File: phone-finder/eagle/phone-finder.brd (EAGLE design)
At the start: 50 x 50 mm, 46 parts, among them J1 MICRO USB, J2 PHONE-JACK, K1 RELAY, Q1 12Mhz, Q2 2N2222, Q3 2N2222, T1 DTA114EET1G (2x10K), U1 AP2114H-3.3TRG1, U2 NUF2042XV6T1G, U3 LPC11U35FHI33/501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

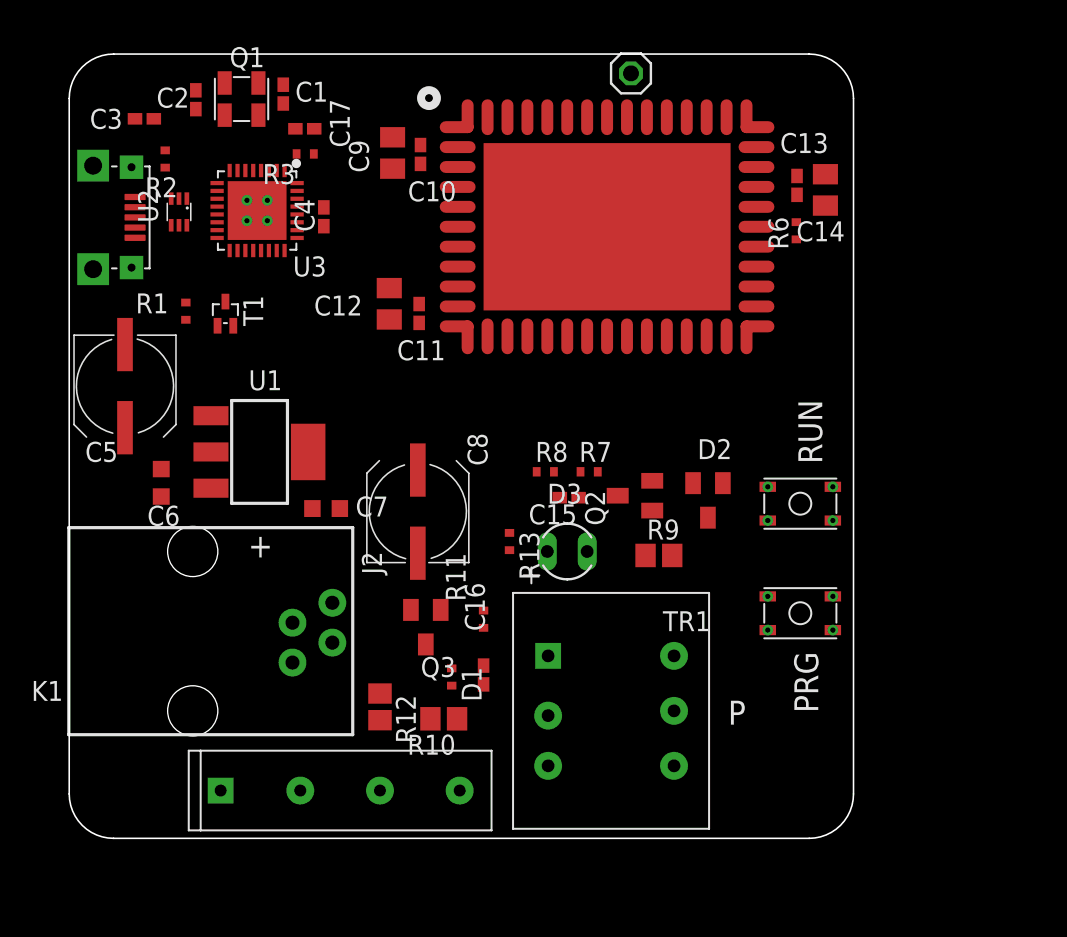
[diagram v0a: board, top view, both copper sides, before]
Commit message: Updated BOM (still needs Mouser part numbers and part references).
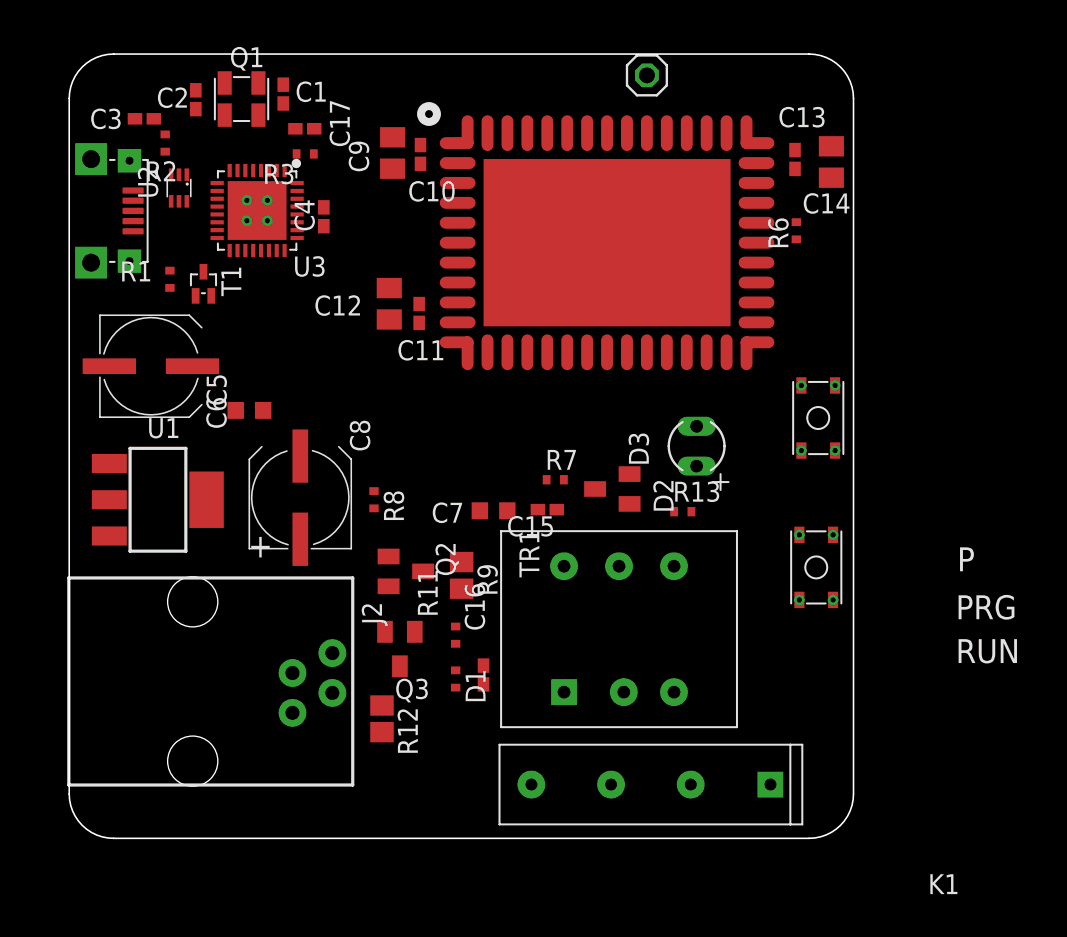
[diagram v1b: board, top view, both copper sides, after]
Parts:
- removed R10: 100, phone-finder:R0805
- moved K1 19.8 mm to (37.1, 3.43), turned to 180 degrees
- moved Q2 15.4 mm to (21.5, 17.0), turned to 270 degrees
- moved R9 12.6 mm to (25.0, 16.8), turned to 270 degrees
- moved R13 11.2 mm to (39.1, 20.8), turned to 0 degrees
- moved R8 11.1 mm to (19.4, 21.6), turned to 270 degrees
- moved C7 10.7 mm to (27.1, 20.9), turned to 0 degrees
- moved D3 10.6 mm to (40.0, 25.0), turned to 90 degrees
- moved C8 7.55 mm to (14.7, 21.7)
- moved C6 7.28 mm to (11.5, 27.3), turned to 0 degrees
- moved U1 7.16 mm to (5.66, 21.6)
- moved D2 6.14 mm to (34.6, 22.3), turned to 90 degrees
- moved S2 5.58 mm to (47.8, 26.8), turned to 90 degrees
- moved TR1 5.23 mm to (35.1, 13.3), turned to 270 degrees
- moved J2 3.21 mm to (7.87, 10.0)
- moved S1 3.09 mm to (47.6, 17.3), turned to 270 degrees
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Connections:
- removed net N$15: D1.2, R10.2, R12.1
- net N$9: now also D1.2, R12.1; no longer R10.1
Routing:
- net GND: track 0.00 -> 33.5 mm

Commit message: PCB layout in progress.
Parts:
- moved C7 18.2 mm to (9.65, 26.2), turned to 180 degrees
- moved C6 6.17 mm to (5.40, 26.3), turned to 180 degrees
- moved C3 4.89 mm to (9.62, 45.1)
- moved S2 4.83 mm to (47.8, 22.0)
- moved K1 4.06 mm to (33.0, 3.43)
- moved S1 3.94 mm to (47.6, 13.3)
- moved C2 2.71 mm to (10.7, 47.6)
- moved R1 2.37 mm to (7.41, 37.8), turned to 0 degrees
- moved R2 2.25 mm to (7.62, 42.6), turned to 0 degrees
- moved Q1 2.19 mm to (13.1, 47.5)
- moved C1 2.04 mm to (15.7, 47.6)
- moved C11 1.21 mm to (22.4, 32.3)
- moved U2 1.17 mm to (7.25, 40.3)
- moved R6 1.14 mm to (46.4, 39.9)
- moved R3 0.92 mm to (15.9, 43.9)
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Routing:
- net GND: track 33.5 -> 358.0 mm, vias 0 -> 18
- net +3V3: track 0.00 -> 43.0 mm, vias 0 -> 6
- net +5V: track 0.00 -> 34.0 mm, vias 0 -> 4
- net N$1: track 0.00 -> 8.47 mm
- net N$6: track 0.00 -> 6.94 mm
- net N$3: track 0.00 -> 6.16 mm
- net USB_DM: track 0.00 -> 5.23 mm
- net N$12: track 0.00 -> 3.87 mm
- net N$2: track 0.00 -> 3.43 mm
- net USB_DP: track 0.00 -> 3.13 mm
- net WIFI_IRQ: track 0.00 -> 1.28 mm, vias 0 -> 1
- net LED: track 0.00 -> 1.20 mm, vias 0 -> 1
- added copper zone on layer 16, net GND

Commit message: Layout work in progress.
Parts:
- moved R12 23.9 mm to (43.4, 3.17), turned to 180 degrees
- moved D1 18.6 mm to (42.8, 6.35)
- moved C16 18.5 mm to (44.5, 6.22)
- moved R7 8.91 mm to (22.1, 21.7), turned to 180 degrees
- moved C15 8.58 mm to (22.1, 18.9), turned to 0 degrees
- moved R9 5.10 mm to (27.3, 21.3), turned to 180 degrees
- moved R11 3.87 mm to (21.0, 11.8), turned to 180 degrees
- moved R13 3.76 mm to (36.0, 23.0)
- moved K1 3.43 mm to (29.6, 3.43)
- moved D2 3.20 mm to (31.9, 23.9)
- moved Q3 3.18 mm to (21.8, 8.97), turned to 90 degrees
- moved R8 3.00 mm to (22.1, 20.3), turned to 180 degrees
- moved R3 2.13 mm to (18.0, 44.5)
- moved R6 1.94 mm to (48.3, 39.5), turned to 270 degrees
- moved C17 1.85 mm to (17.7, 45.7)
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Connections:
- removed net N$20: K1.4, R12.2
- new net N$15: K1.1, R12.2
- net +3V3: no longer U1.2
- net N$11: now also K1.4; no longer K1.1
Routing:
- net +3V3: track 43.0 -> 95.5 mm, vias 6 -> 8
- net GND: track 358.0 -> 385.3 mm, vias 18 -> 22
- net +5V: track 34.0 -> 32.9 mm
- net N$6: track 6.94 -> 6.24 mm
- net N$12: track 3.87 -> 3.35 mm

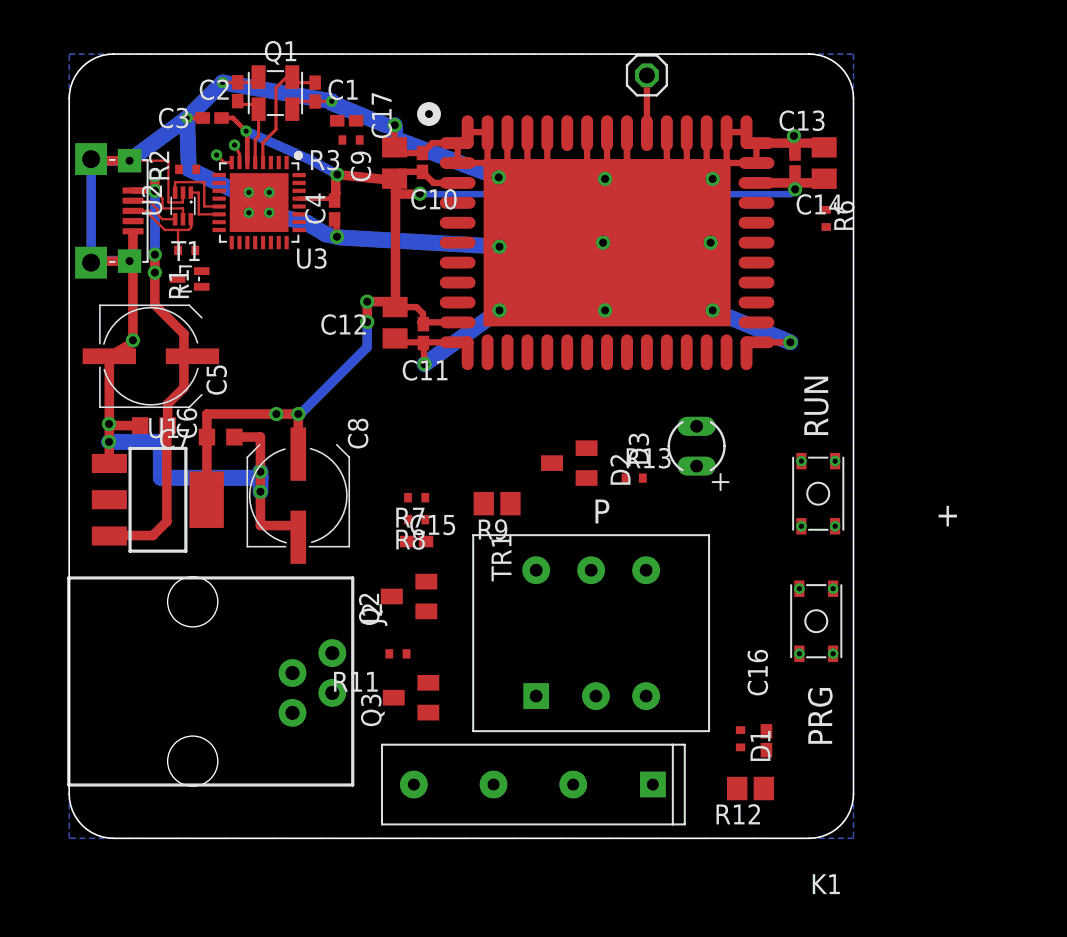
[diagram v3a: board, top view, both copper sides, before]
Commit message: Critical net routing done.
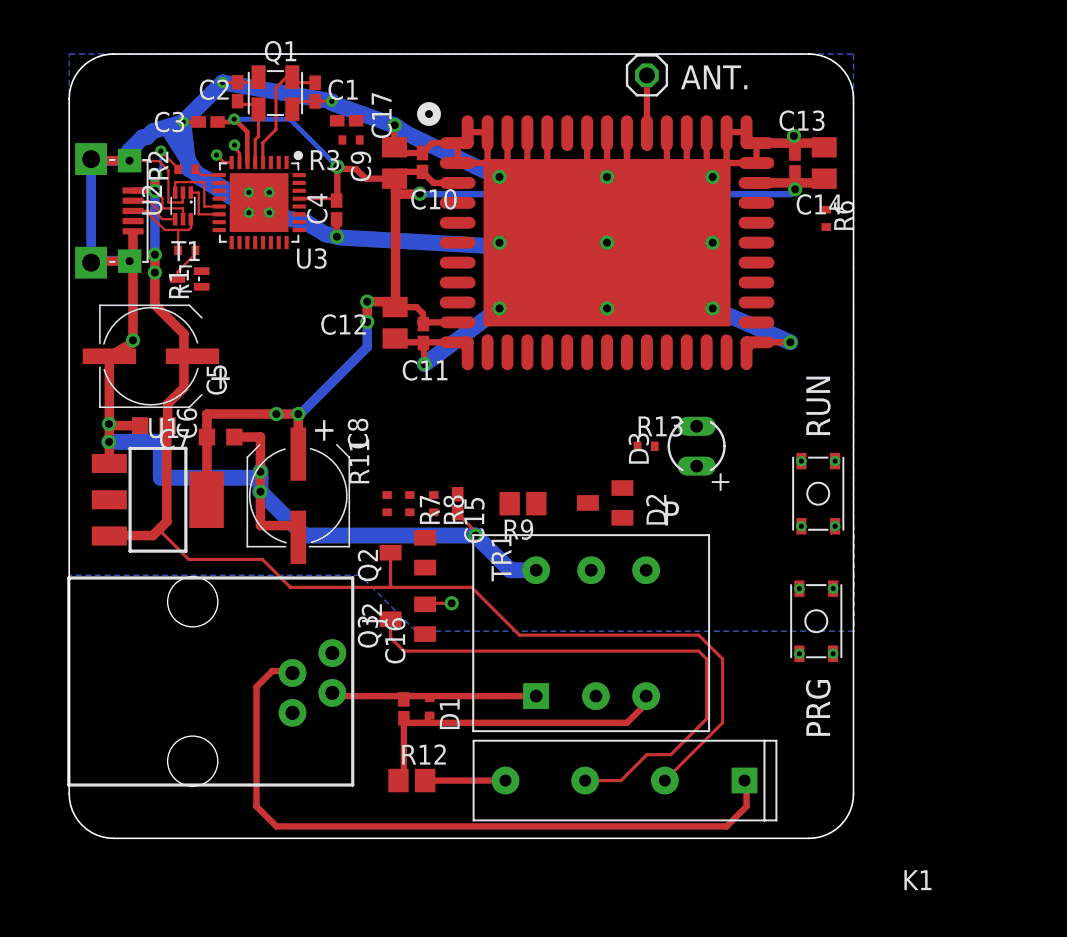
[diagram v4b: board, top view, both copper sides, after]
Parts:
- moved C16 23.2 mm to (21.3, 8.26)
- moved R12 21.6 mm to (21.8, 3.68), turned to 0 degrees
- moved D1 19.9 mm to (23.0, 8.38)
- moved R11 9.60 mm to (20.3, 21.3), turned to 90 degrees
- moved K1 5.85 mm to (35.4, 3.68)
- moved Q3 5.01 mm to (21.6, 14.0)
- moved C15 3.56 mm to (24.8, 21.3), turned to 270 degrees
- moved D2 3.42 mm to (34.2, 21.4)
- moved Q2 2.80 mm to (21.6, 18.2)
- moved R13 2.17 mm to (36.8, 25.0)
- moved R9 1.65 mm to (28.9, 21.3)
- moved R8 1.49 mm to (23.2, 21.3), turned to 270 degrees
- moved R7 0.58 mm to (21.7, 21.3), turned to 270 degrees
- moved C3 0.36 mm to (8.86, 45.7)
- moved C4 0.13 mm to (17.0, 40.1)
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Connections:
- net N$11: now also K1.1; no longer K1.4
- net N$15: now also K1.4; no longer K1.1
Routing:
- net +5V: track 32.9 -> 87.2 mm, vias 4 -> 5
- net N$11: track 0.00 -> 44.2 mm
- net N$4: track 0.00 -> 35.1 mm
- net GND: track 385.3 -> 419.8 mm, vias 22 -> 24
- net N$9: track 0.00 -> 21.2 mm
- net N$10: track 0.00 -> 13.6 mm
- net N$15: track 0.00 -> 5.12 mm
- net N$5: track 0.00 -> 2.29 mm
- net +3V3: track 95.5 -> 97.5 mm
- net VBUS: track 0.00 -> 1.67 mm
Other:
- board text added: "ANT."

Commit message: Cleaned up component references.
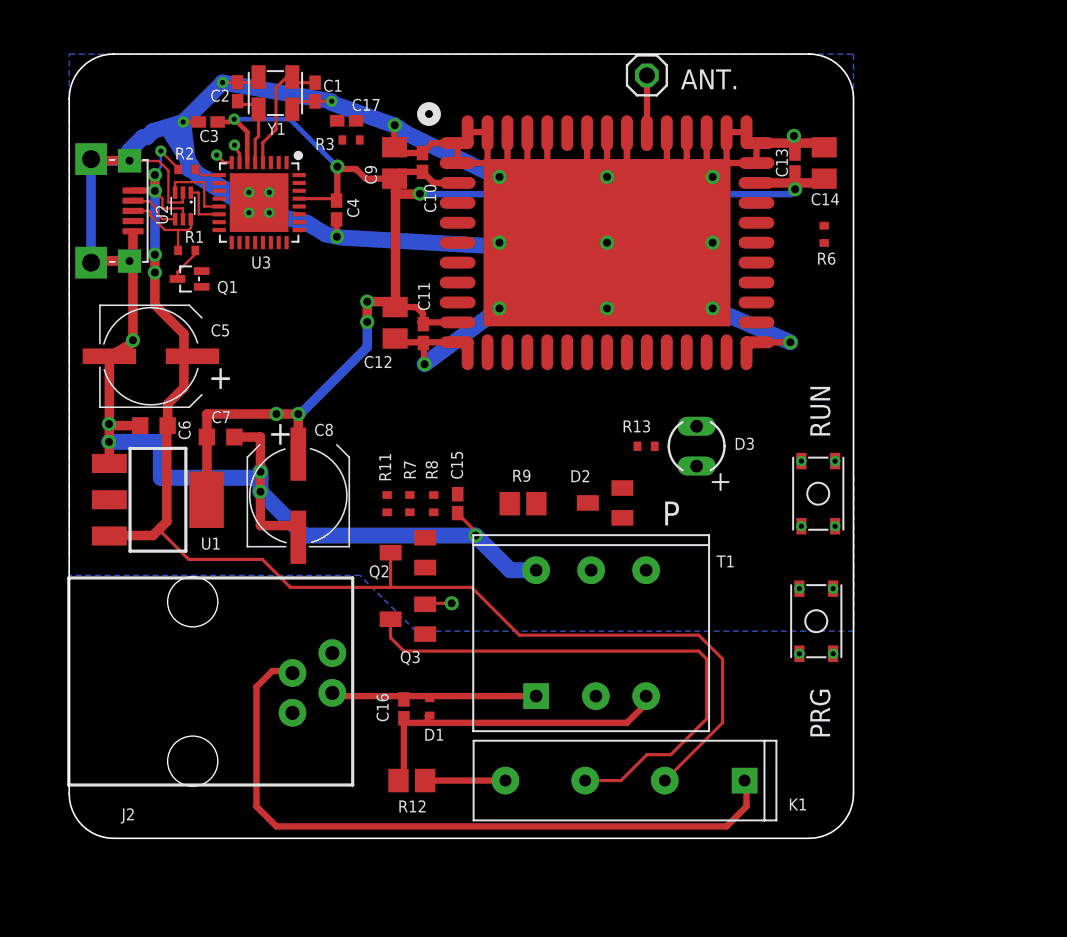
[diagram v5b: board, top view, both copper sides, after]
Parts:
- removed TR1: TRANSFORMER, phone-finder:TRANSFORMER
- added Y1: 12Mhz, phone-finder:CRYSTAL
- Q1: value 12Mhz -> DTA114EET1G (2x10K); device phone-finder:CRYSTAL -> phone-finder:SC75-BEC
- T1: value DTA114EET1G (2x10K) -> TRANSFORMER; device phone-finder:SC75-BEC -> phone-finder:TRANSFORMER
- moved T1 34.1 mm to (33.3, 13.1), turned to 270 degrees
- moved Q1 13.1 mm to (7.67, 35.7), turned to 90 degrees
- moved R6 1.02 mm to (48.1, 38.5)
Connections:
- net +3V3: now also Q1.E; no longer T1.E
- net GND: now also T1.6, Y1.2, Y1.4; no longer Q1.2, Q1.4, TR1.6
- net N$1: now also Y1.3; no longer Q1.3
- net N$10: now also T1.1; no longer TR1.1
- net N$17: now also T1.4; no longer TR1.4
- net N$3: now also Y1.1; no longer Q1.1
- net N$5: now also Q1.C; no longer T1.C
- net N$9: now also T1.3; no longer TR1.3
- net USB_CONNECT: now also Q1.B; no longer T1.B

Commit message: Added board label.
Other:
- board text added: "PHONE FINDER V1.0"
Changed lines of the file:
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@@
 <board>
 <plain>
-<text x="48.514" y="6.35" size="1.27" layer="21" font="vector" ratio="10" rot="R90">PRG</text>
-<text x="48.514" y="25.527" size="1.27" layer="21" font="vector" ratio="10" rot="R90">RUN</text>
+<text x="48.26" y="7.747" size="1.016" layer="21" font="vector" ratio="10" rot="R90">PRG</text>
+<text x="48.133" y="25.527" size="1.016" layer="21" font="vector" ratio="10" rot="R90">RUN</text>
 <text x="12.6746" y="25.0952" size="1.524" layer="21" font="vector" ratio="10">+</text>
 <wire x1="50" y1="2.828425" x2="50" y2="47.171575" width="0.1016" layer="20"/>
@@
 <wire x1="21.336" y1="10.922" x2="53.213" y2="10.922" width="0.2032" layer="42"/>
 <text x="8.8646" y="28.6512" size="1.524" layer="21" font="vector" ratio="10">+</text>
-<text x="38.989" y="47.752" size="1.27" layer="21" font="vector" ratio="10">ANT.</text>
+<text x="38.989" y="47.752" size="1.016" layer="21" font="vector" ratio="10">ANT.</text>
+<text x="3.302" y="1.143" size="1.016" layer="21" font="vector" ratio="10">PHONE FINDER V1.0</text>
 </plain>
 <attributes>
@@
 <attribute name="MF" value="" x="7.874" y="10" size="1.778" layer="27" rot="R270" display="off"/>
 <attribute name="OC_FARNELL" value="unknown" x="7.874" y="10" size="1.778" layer="27" rot="R270" display="off"/>
-<attribute name="NAME" x="3.335" y="1.143" size="0.762" layer="25" font="vector" ratio="10"/>
+<attribute name="NAME" x="18.702" y="10.668" size="0.762" layer="25" font="vector" ratio="10"/>
 </element>
 <element name="D3" library="phone-finder" package="LED" value="LED" x="40" y="25" smashed="yes" rot="R90">

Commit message: Work in progress. Minor tweaks.
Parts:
- moved R13 0.54 mm to (36.4, 25.4)
- turned D3 to 270 degrees
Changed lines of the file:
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@@
 <attribute name="NAME" x="19.615" y="41.676" size="0.762" layer="25" font="vector" ratio="10" rot="R90"/>
 </element>
-<element name="U4" library="phone-finder" package="WIFI_MODULE" value="AMW006" x="24.13" y="30.353" smashed="yes"/>
+<element name="U4" library="phone-finder" package="WIFI_MODULE" value="AMW006" x="24.13" y="30.353"/>
 <element name="C13" library="phone-finder" package="C0402K" value="0.1uF" x="46.271" y="43.053" smashed="yes" rot="R90">
 <attribute name="NAME" x="45.817" y="42.143" size="0.762" layer="25" font="vector" ratio="10" rot="R90"/>
@@
 <attribute name="NAME" x="18.702" y="10.668" size="0.762" layer="25" font="vector" ratio="10"/>
 </element>
-<element name="D3" library="phone-finder" package="LED" value="LED" x="40" y="25" smashed="yes" rot="R90">
-<attribute name="NAME" x="42.399" y="24.77" size="0.762" layer="25" font="vector" ratio="10"/>
-</element>
-<element name="R13" library="phone-finder" package="R0402" value="1K5" x="36.7792" y="24.9936" smashed="yes">
-<attribute name="NAME" x="35.2552" y="25.8826" size="0.762" layer="25" font="vector" ratio="10"/>
+<element name="D3" library="phone-finder" package="LED" value="LED" x="40" y="25" smashed="yes" rot="R270">
+<attribute name="NAME" x="42.282" y="25.697" size="0.762" layer="25" font="vector" ratio="10"/>
+</element>
+<element name="R13" library="phone-finder" package="R0402" value="1K5" x="36.3982" y="25.3746" smashed="yes">
+<attribute name="NAME" x="34.1122" y="26.1366" size="0.762" layer="25" font="vector" ratio="10"/>
 </element>
 </elements>
@@
 <wire x1="10.857" y1="43.626" x2="10.541" y2="44.196" width="0.2032" layer="1"/>
 <via x="10.541" y="44.196" extent="1-16" drill="0.3302"/>
-<wire x1="10.857" y1="43.082" x2="36.2292" y2="24.9936" width="0" layer="19" extent="1-1"/>
+<wire x1="10.857" y1="43.082" x2="35.8482" y2="25.3746" width="0" layer="19" extent="1-1"/>
 </signal>
 <signal name="N$14">
 <contactref element="R13" pad="2"/>
 <contactref element="D3" pad="A"/>
-<wire x1="37.3292" y1="24.9936" x2="40" y2="23.73" width="0" layer="19" extent="1-1"/>
+<wire x1="36.9482" y1="25.3746" x2="40" y2="26.27" width="0" layer="19" extent="1-1"/>
 </signal>
 <signal name="GND1">
